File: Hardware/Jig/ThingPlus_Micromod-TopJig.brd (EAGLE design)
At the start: 104.1 x 35.6 mm, 9 parts

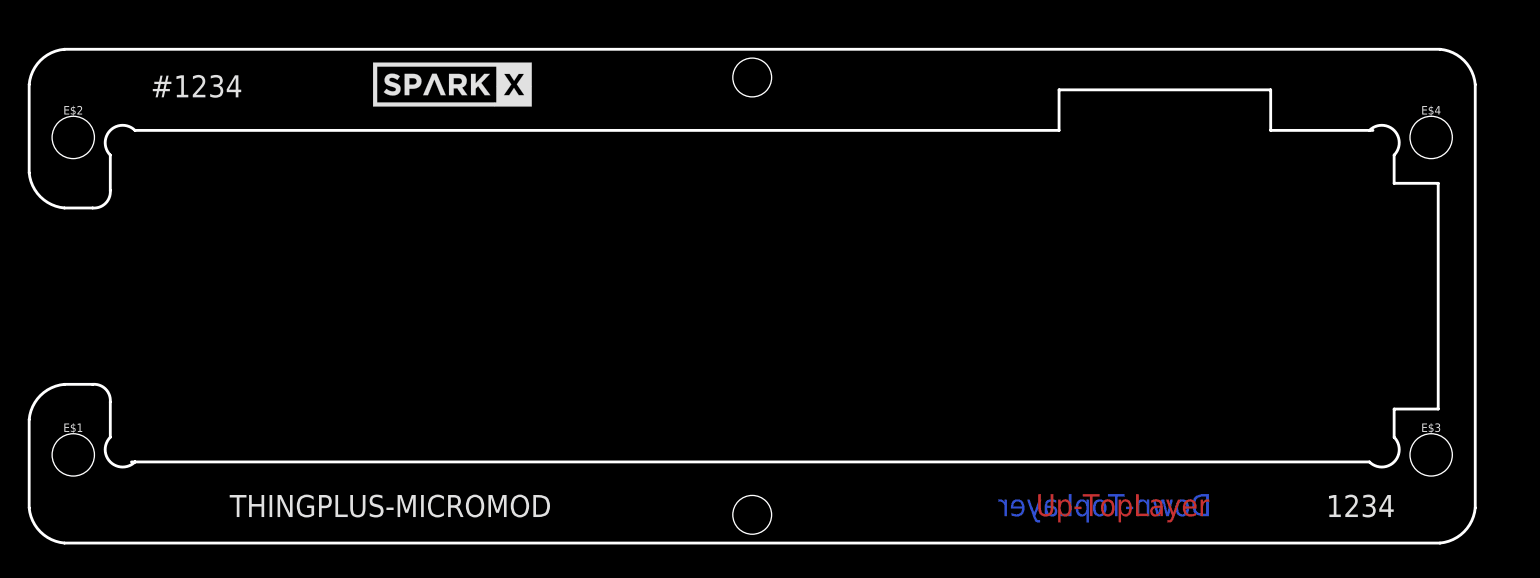
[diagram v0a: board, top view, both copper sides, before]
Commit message: Added jig number, SKU and board names to test jig.
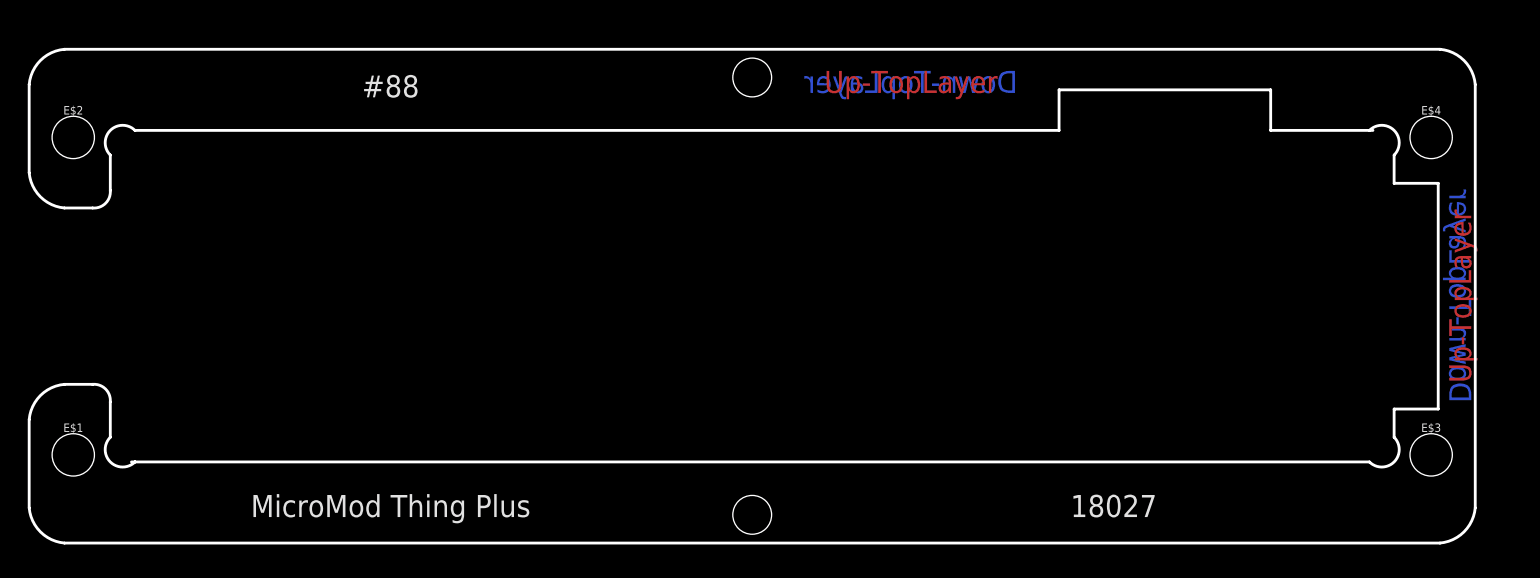
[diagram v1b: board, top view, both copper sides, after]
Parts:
- removed U$1, U$2: SPARKX-LOGO5, SparkX:SPARKX-LARGE
- moved FRAME1 7.62 mm to (24.4, 30.2)
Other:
- board text added: "#88"
- board text added: "18027"
- board text added: "MicroMod Thing Plus"
- board text removed: "#1234"
- board text removed: "1234"
- board text removed: "THINGPLUS-MICROMOD"
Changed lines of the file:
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@@
 <layer number="47" name="Measures" color="7" fill="1" visible="no" active="yes"/>
 <layer number="48" name="Document" color="7" fill="1" visible="no" active="yes"/>
-<layer number="49" name="Reference" color="7" fill="1" visible="yes" active="yes"/>
+<layer number="49" name="Reference" color="7" fill="1" visible="no" active="yes"/>
 <layer number="50" name="dxf" color="7" fill="1" visible="no" active="yes"/>
 <layer number="51" name="tDocu" color="6" fill="1" visible="yes" active="yes"/>
@@
 <layer number="56" name="wert" color="7" fill="1" visible="no" active="no"/>
 <layer number="57" name="tCAD" color="7" fill="1" visible="no" active="no"/>
-<layer number="58" name="bCAD" color="7" fill="1" visible="no" active="no"/>
 <layer number="59" name="tCarbon" color="7" fill="1" visible="no" active="no"/>
 <layer number="60" name="bCarbon" color="7" fill="1" visible="no" active="no"/>
@@
 <dimension x1="0" y1="-1.27" x2="91.44" y2="-1.27" x3="45.72" y3="-7.62" textsize="1.778" textratio="15" layer="47" unit="inch"/>
 <dimension x1="-1.27" y1="0" x2="-1.27" y2="22.86" x3="-7.62" y3="11.43" textsize="1.778" textratio="15" layer="47" unit="inch"/>
-<text x="50.8" y="37.846" size="1.778" layer="51" font="vector" ratio="15">Ricardo R.</text>
+<text x="50.8" y="30.226" size="1.778" layer="51" font="vector" ratio="15">Ricardo R.</text>
 <wire x1="-0.508" y1="21.59" x2="1.27" y2="23.368" width="0.2032" layer="20" curve="-180"/>
 <wire x1="1.27" y1="23.368" x2="67.818" y2="23.368" width="0.2032" layer="20"/>
@@
 <wire x1="-1.778" y1="17.78" x2="-0.508" y2="19.05" width="0.2032" layer="20" curve="100"/>
 <wire x1="-0.508" y1="19.05" x2="-0.508" y2="21.59" width="0.2032" layer="20"/>
-<text x="5.715" y="26.543" size="1.5875" layer="21" font="vector" ratio="15" align="center">#1234</text>
-<text x="19.685" y="-3.683" size="1.5875" layer="21" font="vector" ratio="15" align="center">THINGPLUS-MICROMOD</text>
-<text x="89.535" y="-3.683" size="1.5875" layer="21" font="vector" ratio="15" align="center">1234</text>
-<text x="72.39" y="-3.6195" size="1.5875" layer="1" font="vector" ratio="15" rot="R180" align="center">Up-TopLayer</text>
-<text x="71.12" y="-3.6195" size="1.5875" layer="16" font="vector" ratio="15" rot="MR0" align="center">Down-TopLayer</text>
+<text x="19.685" y="26.543" size="1.5875" layer="21" font="vector" ratio="15" align="center">#88</text>
+<text x="19.685" y="-3.683" size="1.5875" layer="21" font="vector" ratio="15" align="center">MicroMod Thing Plus</text>
+<text x="71.755" y="-3.683" size="1.5875" layer="21" font="vector" ratio="15" align="center">18027</text>
+<text x="96.7105" y="11.43" size="1.5875" layer="1" font="vector" ratio="15" rot="R90" align="center">Up-TopLayer</text>
+<text x="96.7105" y="11.43" size="1.5875" layer="16" font="vector" ratio="15" rot="MR90" align="center">Down-TopLayer</text>
+<text x="57.15" y="26.8605" size="1.5875" layer="1" font="vector" ratio="15" rot="R180" align="center">Up-TopLayer</text>
+<text x="57.15" y="26.8605" size="1.5875" layer="16" font="vector" ratio="15" rot="MR0" align="center">Down-TopLayer</text>
 </plain>
 <attributes>
@@
 </autorouter>
 <elements>
-<element name="FRAME1" library="SparkFun-Aesthetics" package="CREATIVE_COMMONS" value="FRAME-LEDGER" x="24.384" y="37.846" smashed="yes">
-<attribute name="DESIGNER" value="Ricardo R." x="104.394" y="-2.794" size="1.778" layer="27" display="off"/>
-<attribute name="REV" value="" x="104.394" y="-2.794" size="1.778" layer="27" display="off"/>
+<element name="FRAME1" library="SparkFun-Aesthetics" package="CREATIVE_COMMONS" value="FRAME-LEDGER" x="24.384" y="30.226" smashed="yes">
+<attribute name="DESIGNER" value="Ricardo R." x="104.394" y="-10.414" size="1.778" layer="27" display="off"/>
+<attribute name="REV" value="" x="104.394" y="-10.414" size="1.778" layer="27" display="off"/>
 </element>
 <element name="E$1" library="SparkFun-Hardware" package="STAND-OFF-TIGHT" value="" x="-3.175" y="0" smashed="yes">
@@
 <element name="E$5" library="SparkFun-Hardware" package="NUBBIN_LOCKER" value="" x="45.72" y="-4.318" smashed="yes"/>
 <element name="E$6" library="SparkFun-Hardware" package="NUBBIN_LOCKER" value="" x="45.72" y="27.178" smashed="yes"/>
-<element name="U$1" library="SparkX" package="SPARKX-LARGE" value="SPARKX-LOGO5" x="24.13" y="26.67" smashed="yes"/>
-<element name="U$2" library="SparkX" package="SPARKX-LARGE" value="SPARKX-LOGO5" x="24.13" y="26.67" smashed="yes" rot="MR0"/>
 </elements>
 <signals>

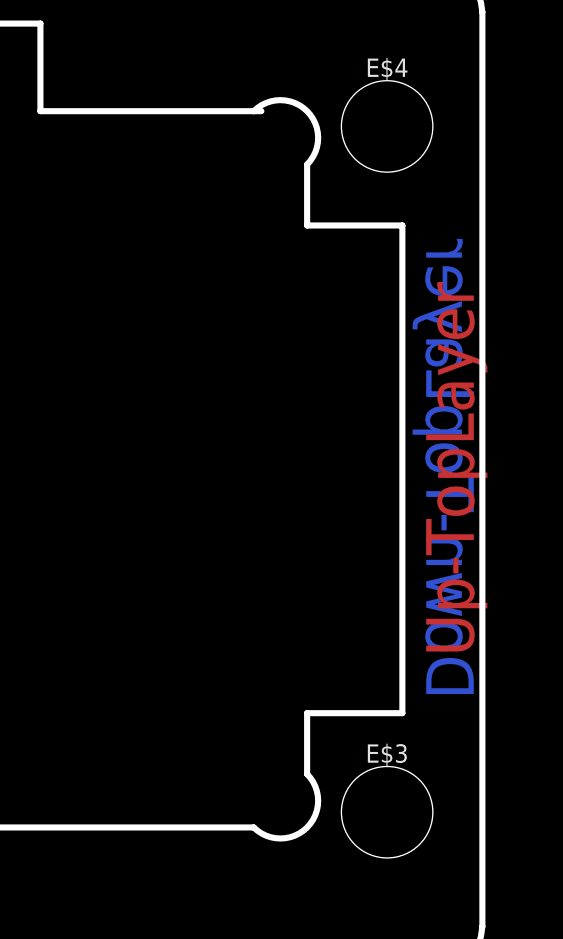
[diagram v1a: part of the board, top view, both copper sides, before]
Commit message: Added milling polygons to bottom and middle jig boards; created Gerber files.
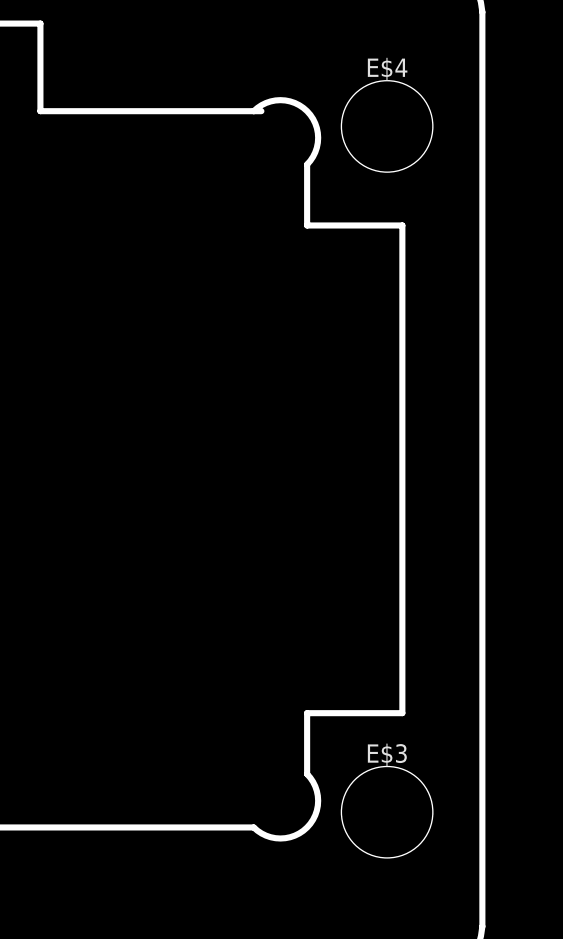
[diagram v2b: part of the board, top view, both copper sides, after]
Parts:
- moved FRAME1 1.80 mm to (23.1, 31.5)
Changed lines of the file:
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@@
 <drawing>
 <settings>
-<setting alwaysvectorfont="yes"/>
+<setting alwaysvectorfont="no"/>
 <setting verticaltext="up"/>
 </settings>
@@
 <dimension x1="0" y1="-1.27" x2="91.44" y2="-1.27" x3="45.72" y3="-7.62" textsize="1.778" textratio="15" layer="47" unit="inch"/>
 <dimension x1="-1.27" y1="0" x2="-1.27" y2="22.86" x3="-7.62" y3="11.43" textsize="1.778" textratio="15" layer="47" unit="inch"/>
-<text x="50.8" y="30.226" size="1.778" layer="51" font="vector" ratio="15">Ricardo R.</text>
+<text x="50.8" y="31.496" size="1.778" layer="51" font="vector" ratio="15">Ricardo R.</text>
 <wire x1="-0.508" y1="21.59" x2="1.27" y2="23.368" width="0.2032" layer="20" curve="-180"/>
 <wire x1="1.27" y1="23.368" x2="67.818" y2="23.368" width="0.2032" layer="20"/>
@@
 <text x="19.685" y="-3.683" size="1.5875" layer="21" font="vector" ratio="15" align="center">MicroMod Thing Plus</text>
 <text x="71.755" y="-3.683" size="1.5875" layer="21" font="vector" ratio="15" align="center">18027</text>
-<text x="96.7105" y="11.43" size="1.5875" layer="1" font="vector" ratio="15" rot="R90" align="center">Up-TopLayer</text>
-<text x="96.7105" y="11.43" size="1.5875" layer="16" font="vector" ratio="15" rot="MR90" align="center">Down-TopLayer</text>
 <text x="57.15" y="26.8605" size="1.5875" layer="1" font="vector" ratio="15" rot="R180" align="center">Up-TopLayer</text>
 <text x="57.15" y="26.8605" size="1.5875" layer="16" font="vector" ratio="15" rot="MR0" align="center">Down-TopLayer</text>
@@
 </autorouter>
 <elements>
-<element name="FRAME1" library="SparkFun-Aesthetics" package="CREATIVE_COMMONS" value="FRAME-LEDGER" x="24.384" y="30.226" smashed="yes">
-<attribute name="DESIGNER" value="Ricardo R." x="104.394" y="-10.414" size="1.778" layer="27" display="off"/>
-<attribute name="REV" value="" x="104.394" y="-10.414" size="1.778" layer="27" display="off"/>
+<element name="FRAME1" library="SparkFun-Aesthetics" package="CREATIVE_COMMONS" value="FRAME-LEDGER" x="23.114" y="31.496" smashed="yes">
+<attribute name="DESIGNER" value="Ricardo R." x="103.124" y="-9.144" size="1.778" layer="27" display="off"/>
+<attribute name="REV" value="" x="103.124" y="-9.144" size="1.778" layer="27" display="off"/>
 </element>
 <element name="E$1" library="SparkFun-Hardware" package="STAND-OFF-TIGHT" value="" x="-3.175" y="0" smashed="yes">

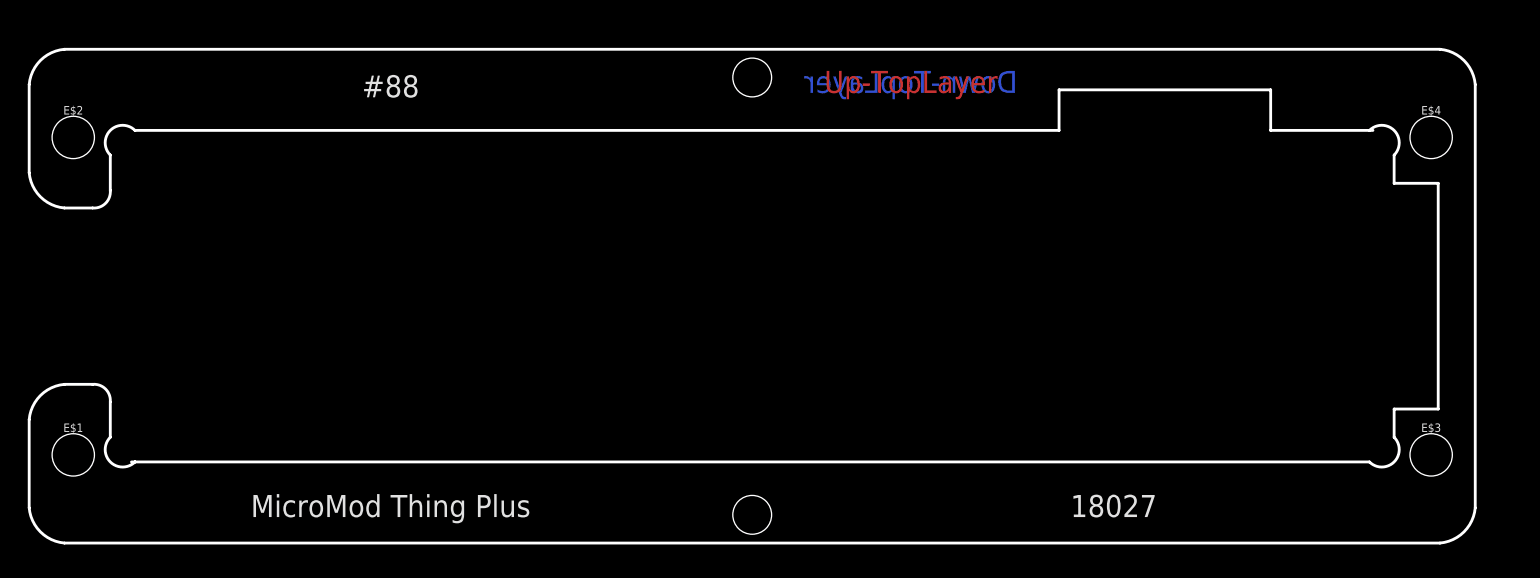
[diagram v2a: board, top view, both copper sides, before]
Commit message: Enlarged right board edge per JLCPCB request
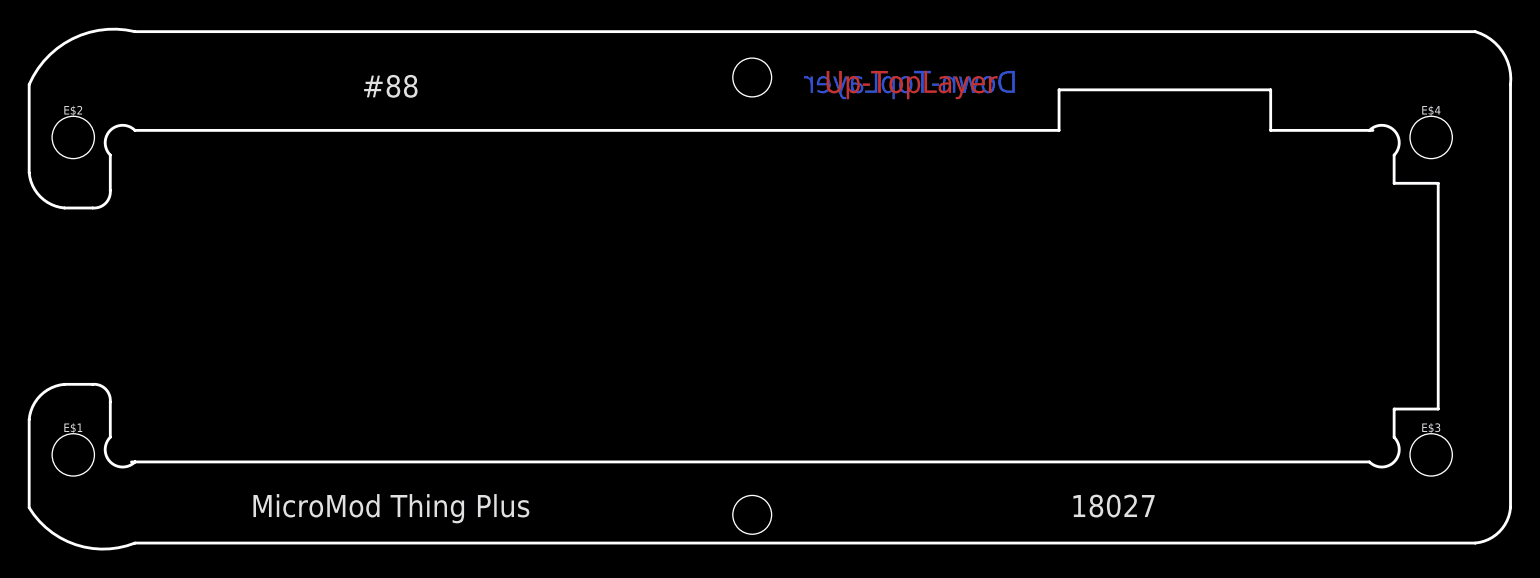
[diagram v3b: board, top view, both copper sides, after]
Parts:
- moved FRAME1 5.24 mm to (21.8, 36.6)
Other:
- board size 104.1 x 35.6 mm -> 106.7 x 37.4 mm
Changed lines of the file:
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@@
 <dimension x1="0" y1="-1.27" x2="91.44" y2="-1.27" x3="45.72" y3="-7.62" textsize="1.778" textratio="15" layer="47" unit="inch"/>
 <dimension x1="-1.27" y1="0" x2="-1.27" y2="22.86" x3="-7.62" y3="11.43" textsize="1.778" textratio="15" layer="47" unit="inch"/>
-<text x="50.8" y="31.496" size="1.778" layer="51" font="vector" ratio="15">Ricardo R.</text>
+<text x="49.53" y="36.576" size="1.778" layer="51" font="vector" ratio="15">Ricardo R.</text>
 <wire x1="-0.508" y1="21.59" x2="1.27" y2="23.368" width="0.2032" layer="20" curve="-180"/>
 <wire x1="1.27" y1="23.368" x2="67.818" y2="23.368" width="0.2032" layer="20"/>
@@
 <wire x1="-3.81" y1="5.08" x2="-6.35" y2="2.54" width="0.2032" layer="20" curve="80"/>
 <wire x1="-6.35" y1="2.54" x2="-6.35" y2="-3.81" width="0.2032" layer="20"/>
-<wire x1="-6.35" y1="-3.81" x2="-3.81" y2="-6.35" width="0.2032" layer="20" curve="80"/>
-<wire x1="-3.81" y1="-6.35" x2="95.25" y2="-6.35" width="0.2032" layer="20"/>
-<wire x1="95.25" y1="-6.35" x2="97.79" y2="-3.81" width="0.2032" layer="20" curve="80"/>
-<wire x1="97.79" y1="-3.81" x2="97.79" y2="26.67" width="0.2032" layer="20"/>
-<wire x1="97.79" y1="26.67" x2="95.25" y2="29.21" width="0.2032" layer="20" curve="80"/>
-<wire x1="95.25" y1="29.21" x2="-3.81" y2="29.21" width="0.2032" layer="20"/>
-<wire x1="-3.81" y1="29.21" x2="-6.35" y2="26.67" width="0.2032" layer="20" curve="80"/>
+<wire x1="-6.35" y1="-3.81" x2="1.27" y2="-6.35" width="0.2032" layer="20" curve="80"/>
+<wire x1="1.27" y1="-6.35" x2="97.79" y2="-6.35" width="0.2032" layer="20"/>
+<wire x1="97.79" y1="-6.35" x2="100.33" y2="-3.81" width="0.2032" layer="20" curve="80"/>
+<wire x1="100.33" y1="-3.81" x2="100.33" y2="26.67" width="0.2032" layer="20"/>
+<wire x1="100.33" y1="26.67" x2="97.79" y2="30.48" width="0.2032" layer="20" curve="80"/>
+<wire x1="97.79" y1="30.48" x2="1.27" y2="30.48" width="0.2032" layer="20"/>
+<wire x1="1.27" y1="30.48" x2="-6.35" y2="26.67" width="0.2032" layer="20" curve="80"/>
 <wire x1="-6.35" y1="26.67" x2="-6.35" y2="20.32" width="0.2032" layer="20"/>
 <wire x1="-6.35" y1="20.32" x2="-3.81" y2="17.78" width="0.2032" layer="20" curve="80"/>
@@
 </autorouter>
 <elements>
-<element name="FRAME1" library="SparkFun-Aesthetics" package="CREATIVE_COMMONS" value="FRAME-LEDGER" x="23.114" y="31.496" smashed="yes">
-<attribute name="DESIGNER" value="Ricardo R." x="103.124" y="-9.144" size="1.778" layer="27" display="off"/>
-<attribute name="REV" value="" x="103.124" y="-9.144" size="1.778" layer="27" display="off"/>
+<element name="FRAME1" library="SparkFun-Aesthetics" package="CREATIVE_COMMONS" value="FRAME-LEDGER" x="21.844" y="36.576" smashed="yes">
+<attribute name="DESIGNER" value="Ricardo R." x="101.854" y="-4.064" size="1.778" layer="27" display="off"/>
+<attribute name="REV" value="" x="101.854" y="-4.064" size="1.778" layer="27" display="off"/>
 </element>
 <element name="E$1" library="SparkFun-Hardware" package="STAND-OFF-TIGHT" value="" x="-3.175" y="0" smashed="yes">
